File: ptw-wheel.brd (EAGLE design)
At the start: 54 x 45 mm, 4 parts

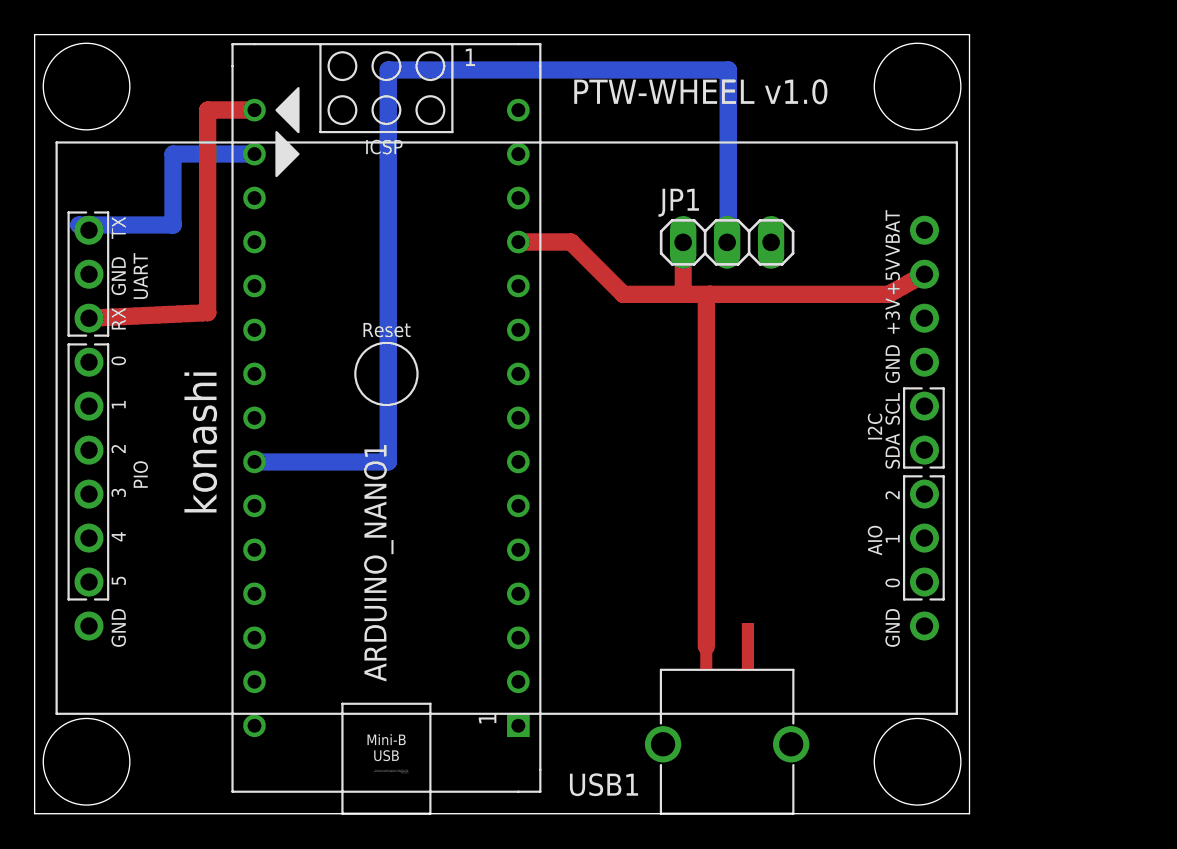
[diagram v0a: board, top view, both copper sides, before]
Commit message: GNDがAirwireになっているのを解消できた！
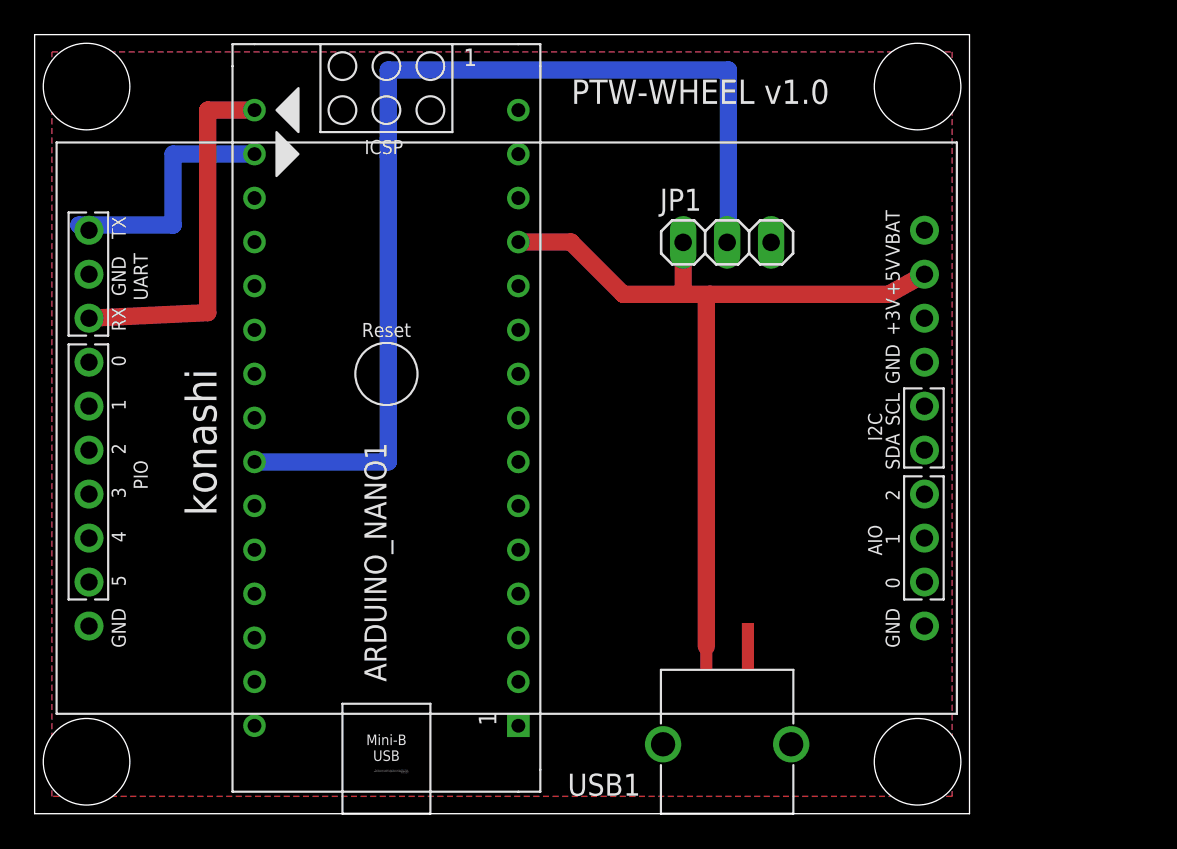
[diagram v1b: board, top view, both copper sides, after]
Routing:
- added copper zone on layer 1, net GND
- added copper zone on layer 16, net GND
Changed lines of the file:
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@@
 <contactref element="U$1" pad="GND@3"/>
 <contactref element="U$1" pad="GND@2"/>
-<wire x1="12.7" y1="33.02" x2="42.54" y2="33" width="0" layer="19" extent="1-16"/>
-<wire x1="42.54" y1="33" x2="51.4" y2="10.84" width="0" layer="19" extent="1-16"/>
-<wire x1="51.4" y1="10.84" x2="51.4" y2="26.08" width="0" layer="19" extent="1-16"/>
-<wire x1="51.4" y1="26.08" x2="3.14" y2="10.84" width="0" layer="19" extent="1-16"/>
-<wire x1="3.14" y1="10.84" x2="41.2" y2="9.66" width="0" layer="19" extent="1-16"/>
-<wire x1="41.2" y1="9.66" x2="43.7" y2="4.01" width="0" layer="19" extent="1-16"/>
-<wire x1="43.7" y1="4.01" x2="36.3" y2="4.01" width="0" layer="19" extent="1-16"/>
-<wire x1="27.94" y1="38.1" x2="3.14" y2="31.16" width="0" layer="19" extent="1-16"/>
+<polygon width="1" layer="16">
+<vertex x="1" y="44"/>
+<vertex x="53" y="44"/>
+<vertex x="53" y="1"/>
+<vertex x="1" y="1"/>
+</polygon>
+<polygon width="1" layer="1">
+<vertex x="1" y="44"/>
+<vertex x="53" y="44"/>
+<vertex x="53" y="1"/>
+<vertex x="1" y="1"/>
+</polygon>
 </signal>
 </signals>

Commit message: 更新
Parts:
- removed U$1: KONASHI2.0, konashiv2-withoud_drill_hole:KONASHI
- added KONASHI: KONASHI2.0, konashiv2-withoud_drill_hole:KONASHI
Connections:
- net +3V: now also KONASHI.+3V; no longer U$1.+3V
- net +5V: now also KONASHI.+5V; no longer U$1.+5V
- net GND: now also KONASHI.GND, KONASHI.GND@1, KONASHI.GND@2, KONASHI.GND@3; no longer U$1.GND, U$1.GND@1, U$1.GND@2, U$1.GND@3
- net N$4: now also KONASHI.TX; no longer U$1.TX
- net N$5: now also KONASHI.RX; no longer U$1.RX
- net VBAT: now also KONASHI.VBAT; no longer U$1.VBAT
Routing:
- removed copper zone on layer 1, net GND
- removed copper zone on layer 16, net GND
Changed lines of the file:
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@@
 <attribute name="VALUE" x="36.19" y="29.825" size="1.27" layer="27"/>
 </element>
-<element name="U$1" library="konashiv2-withoud_drill_hole" package="KONASHI" value="KONASHI2.0" x="26" y="21" smashed="yes" rot="R90"/>
+<element name="KONASHI" library="konashiv2-withoud_drill_hole" package="KONASHI" value="KONASHI2.0" x="25.6" y="21.2" smashed="yes" rot="R90"/>
 <element name="USB1" library="usbcon" package="USBCON" value="USBCON" x="40" y="8.31" smashed="yes" rot="R180">
 <attribute name="NAME" x="35" y="2.31" size="1.27" layer="25" rot="R180"/>
@@
 <signals>
 <signal name="+3V">
-<contactref element="U$1" pad="+3V"/>
+<contactref element="KONASHI" pad="+3V"/>
 </signal>
 <signal name="VBAT">
-<contactref element="U$1" pad="VBAT"/>
+<contactref element="KONASHI" pad="VBAT"/>
 </signal>
 <signal name="VIN">
@@
 </signal>
 <signal name="N$4">
-<contactref element="U$1" pad="TX"/>
+<contactref element="KONASHI" pad="TX"/>
 <contactref element="ARDUINO_NANO1" pad="17"/>
 <wire x1="12.7" y1="38.1" x2="8" y2="38.1" width="1" layer="16"/>
 <wire x1="8" y1="38.1" x2="8" y2="34" width="1" layer="16"/>
-<wire x1="8" y1="34" x2="2.56" y2="34" width="1" layer="16"/>
-<wire x1="2.56" y1="34" x2="3.14" y2="33.7" width="1" layer="16"/>
+<wire x1="8" y1="34" x2="2.546665625" y2="34" width="1" layer="16"/>
+<wire x1="2.546665625" y1="34" x2="2.74" y2="33.9" width="1" layer="16"/>
 </signal>
 <signal name="N$5">
-<contactref element="U$1" pad="RX"/>
+<contactref element="KONASHI" pad="RX"/>
 <contactref element="ARDUINO_NANO1" pad="16"/>
-<wire x1="3.14" y1="28.62" x2="10" y2="28.94" width="1" layer="1"/>
-<wire x1="10" y1="28.94" x2="10" y2="40.629840625" width="1" layer="1"/>
+<wire x1="2.74" y1="28.82" x2="10" y2="29.158659375" width="1" layer="1"/>
+<wire x1="10" y1="29.158659375" x2="10" y2="40.629840625" width="1" layer="1"/>
 <wire x1="10.010159375" y1="40.64" x2="10" y2="40.629840625" width="1" layer="1"/>
 <wire x1="10.010159375" y1="40.64" x2="12.7" y2="40.64" width="1" layer="1"/>
@@
 <signal name="+5V">
 <contactref element="USB1" pad="5V"/>
-<contactref element="U$1" pad="+5V"/>
+<contactref element="KONASHI" pad="+5V"/>
 <contactref element="JP1" pad="1"/>
 <contactref element="ARDUINO_NANO1" pad="12"/>
@@
 <wire x1="37.462459375" y1="32.997540625" x2="37.46" y2="33" width="1" layer="1"/>
 <wire x1="37.462459375" y1="30" x2="39" y2="30" width="1" layer="1"/>
-<wire x1="39" y1="30" x2="49.32" y2="30" width="1" layer="1"/>
-<wire x1="49.32" y1="30" x2="51.4" y2="31.16" width="1" layer="1"/>
+<wire x1="39" y1="30" x2="48.561378125" y2="30" width="1" layer="1"/>
+<wire x1="48.561378125" y1="30" x2="51" y2="31.36" width="1" layer="1"/>
 <wire x1="38.8" y1="9.66" x2="38.8" y2="29.8" width="1" layer="1"/>
 <wire x1="38.8" y1="29.8" x2="39" y2="30" width="1" layer="1"/>
 </signal>
 <signal name="GND">
-<contactref element="U$1" pad="GND"/>
+<contactref element="KONASHI" pad="GND"/>
 <contactref element="USB1" pad="GND"/>
 <contactref element="USB1" pad="SHIELD1"/>
 <contactref element="USB1" pad="SHIELD2"/>
-<contactref element="U$1" pad="GND@1"/>
+<contactref element="KONASHI" pad="GND@1"/>
 <contactref element="JP1" pad="3"/>
 <contactref element="ARDUINO_NANO1" pad="19"/>
 <contactref element="ARDUINO_NANO1" pad="14"/>
-<contactref element="U$1" pad="GND@3"/>
-<contactref element="U$1" pad="GND@2"/>
-<polygon width="1" layer="16">
-<vertex x="1" y="44"/>
-<vertex x="53" y="44"/>
-<vertex x="53" y="1"/>
-<vertex x="1" y="1"/>
-</polygon>
-<polygon width="1" layer="1">
-<vertex x="1" y="44"/>
-<vertex x="53" y="44"/>
-<vertex x="53" y="1"/>
-<vertex x="1" y="1"/>
-</polygon>
+<contactref element="KONASHI" pad="GND@3"/>
+<contactref element="KONASHI" pad="GND@2"/>
+<wire x1="42.54" y1="33" x2="51" y2="26.28" width="0" layer="19" extent="1-1"/>
+<wire x1="51" y1="26.28" x2="51" y2="11.04" width="0" layer="19" extent="1-1"/>
+<wire x1="41.2" y1="9.66" x2="51" y2="11.04" width="0" layer="19" extent="1-1"/>
+<wire x1="43.7" y1="4.01" x2="41.2" y2="9.66" width="0" layer="19" extent="1-1"/>
+<wire x1="36.3" y1="4.01" x2="43.7" y2="4.01" width="0" layer="19" extent="1-1"/>
+<wire x1="27.94" y1="38.1" x2="42.54" y2="33" width="0" layer="19" extent="1-1"/>
+<wire x1="12.7" y1="33.02" x2="27.94" y2="38.1" width="0" layer="19" extent="1-1"/>
+<wire x1="2.74" y1="31.36" x2="12.7" y2="33.02" width="0" layer="19" extent="1-1"/>
+<wire x1="2.74" y1="11.04" x2="2.74" y2="31.36" width="0" layer="19" extent="1-1"/>
 </signal>
 </signals>

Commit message: ボードのレイアウト整理
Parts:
- moved KONASHI 0.13 mm to (25.7, 21.2)
- renumbered ARDUINO_NANO1 to ARDUINO_NANO, USB1 to USB
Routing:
- net GND: track 0.00 -> 133.8 mm
- net N$3: track 60.0 -> 62.2 mm
- added copper zone on layer 1, net GND
- added copper zone on layer 16, net GND
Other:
- board text added: "GND"

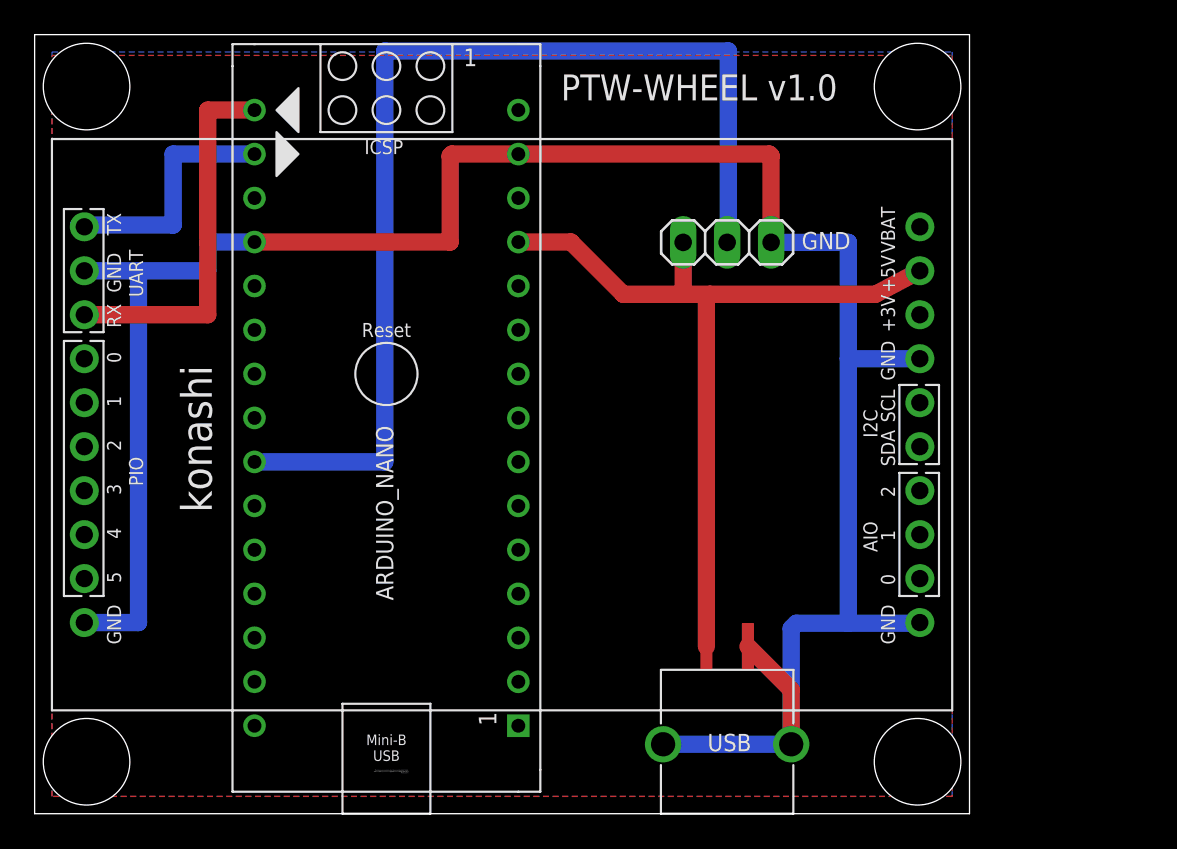
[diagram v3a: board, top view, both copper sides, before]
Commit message: トグルスイッチを追加
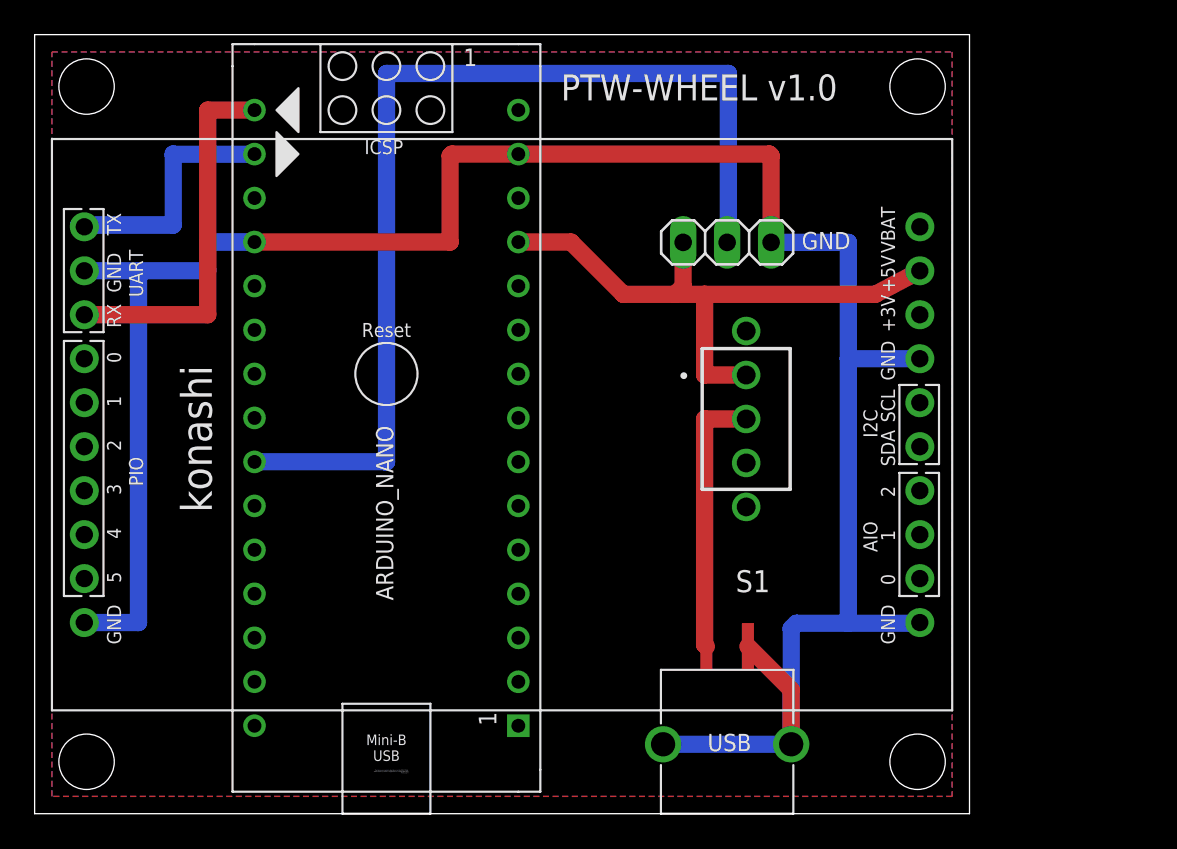
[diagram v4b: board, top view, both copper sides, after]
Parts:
- added S1: 2MS1-T1-B4-M2-Q-E, 2MS1-T1-B4-VS2-Q-E:2MS1-T1-B4-M2-Q-E
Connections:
- new net N$1: S1.2, USB.5V
- net +5V: now also S1.1; no longer USB.5V
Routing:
- net N$1: track 0.00 -> 15.6 mm
- net +5V: track 48.2 -> 35.0 mm
- net N$3: track 62.2 -> 59.6 mm
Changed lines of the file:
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@@
 <layer number="49" name="Reference" color="7" fill="1" visible="yes" active="yes"/>
 <layer number="50" name="dxf" color="12" fill="1" visible="no" active="no"/>
-<layer number="51" name="tDocu" color="7" fill="1" visible="yes" active="yes"/>
+<layer number="51" name="tDocu" color="7" fill="1" visible="no" active="yes"/>
 <layer number="52" name="bDocu" color="7" fill="1" visible="yes" active="yes"/>
 <layer number="53" name="tGND_GNDA" color="7" fill="9" visible="no" active="no"/>
@@
 <wire x1="54" y1="45" x2="0" y2="45" width="0" layer="20"/>
 <wire x1="0" y1="45" x2="0" y2="0" width="0" layer="20"/>
-<hole x="3" y="42" drill="5"/>
-<hole x="3" y="3" drill="5"/>
-<hole x="51" y="3" drill="5"/>
-<hole x="51" y="42" drill="5"/>
+<hole x="3" y="42" drill="3.2"/>
+<hole x="3" y="3" drill="3.2"/>
+<hole x="51" y="3" drill="3.2"/>
+<hole x="51" y="42" drill="3.2"/>
 <text x="30.4" y="41.2" size="1.5" layer="25">PTW-WHEEL v1.0</text>
 <text x="44.3" y="32.6" size="1" layer="25">GND</text>
@@
 <attribute name="NAME" x="41.4" y="4.61" size="1" layer="25" rot="R180"/>
 </element>
+<element name="S1" library="2MS1-T1-B4-VS2-Q-E" package="2MS1-T1-B4-M2-Q-E" value="2MS1-T1-B4-M2-Q-E" x="41.1" y="22.8" smashed="yes" rot="R180">
+<attribute name="DESCRIPTION" value="Sub-miniature toggle switch" x="41.1" y="22.8" size="1" layer="27" rot="R180" display="off"/>
+<attribute name="HEIGHT" value="mm" x="41.1" y="22.8" size="1" layer="27" rot="R180" display="off"/>
+<attribute name="MANUFACTURER_NAME" value="Cosland" x="41.1" y="22.8" size="1" layer="27" rot="R180" display="off"/>
+<attribute name="MANUFACTURER_PART_NUMBER" value="2MS1-T1-B4-M2-Q-E" x="41.1" y="22.8" size="1" layer="27" rot="R180" display="off"/>
+<attribute name="MOUSER_PART_NUMBER" value="" x="41.1" y="22.8" size="1" layer="27" rot="R180" display="off"/>
+<attribute name="MOUSER_PRICE-STOCK" value="" x="41.1" y="22.8" size="1" layer="27" rot="R180" display="off"/>
+<attribute name="NAME" x="41.489" y="13.429" size="1.27" layer="25" rot="R180" align="center"/>
+<attribute name="RS_PART_NUMBER" value="" x="41.1" y="22.8" size="1" layer="27" rot="R180" display="off"/>
+<attribute name="RS_PRICE-STOCK" value="" x="41.1" y="22.8" size="1" layer="27" rot="R180" display="off"/>
+<attribute name="VALUE" x="41.489" y="14.842" size="1.27" layer="27" rot="R180" align="center"/>
+</element>
 </elements>
 <signals>
@@
 <contactref element="JP1" pad="2"/>
 <contactref element="ARDUINO_NANO" pad="24"/>
-<wire x1="12.7" y1="20.32" x2="20.22668125" y2="20.32" width="1" layer="16"/>
-<wire x1="20.22668125" y1="44.05648125" x2="20.22668125" y2="20.32" width="1" layer="16"/>
-<wire x1="20.22668125" y1="44.05648125" x2="40.071040625" y2="44.05648125" width="1" layer="16"/>
-<wire x1="40.071040625" y1="44.05648125" x2="40.071040625" y2="33.071040625" width="1" layer="16"/>
+<wire x1="12.7" y1="20.32" x2="20.32668125" y2="20.32" width="1" layer="16"/>
+<wire x1="20.32668125" y1="42.75648125" x2="20.32668125" y2="20.32" width="1" layer="16"/>
+<wire x1="20.32668125" y1="42.75648125" x2="40.071040625" y2="42.75648125" width="1" layer="16"/>
+<wire x1="40.071040625" y1="42.75648125" x2="40.071040625" y2="33.071040625" width="1" layer="16"/>
 <wire x1="40.071040625" y1="33.071040625" x2="40" y2="33" width="1" layer="16"/>
 </signal>
@@
 </signal>
 <signal name="+5V">
-<contactref element="USB" pad="5V"/>
 <contactref element="KONASHI" pad="+5V"/>
 <contactref element="JP1" pad="1"/>
@@
 <wire x1="27.94" y1="33.02" x2="30.98" y2="33.02" width="1" layer="1"/>
 <wire x1="30.98" y1="33.02" x2="34" y2="30" width="1" layer="1"/>
-<wire x1="34" y1="30" x2="37.462459375" y2="30" width="1" layer="1"/>
-<wire x1="37.462459375" y1="30" x2="37.462459375" y2="32.997540625" width="1" layer="1"/>
-<wire x1="37.462459375" y1="32.997540625" x2="37.46" y2="33" width="1" layer="1"/>
-<wire x1="37.462459375" y1="30" x2="39" y2="30" width="1" layer="1"/>
-<wire x1="39" y1="30" x2="48.561378125" y2="30" width="1" layer="1"/>
-<wire x1="48.561378125" y1="30" x2="51.13" y2="31.36" width="1" layer="1"/>
-<wire x1="38.8" y1="9.66" x2="38.8" y2="29.8" width="1" layer="1"/>
-<wire x1="38.8" y1="29.8" x2="39" y2="30" width="1" layer="1"/>
+<wire x1="51.13" y1="31.36" x2="48.561378125" y2="30" width="1" layer="1"/>
+<contactref element="S1" pad="1"/>
+<wire x1="41.1" y1="25.34" x2="38.701" y2="25.34" width="1" layer="1"/>
+<wire x1="48.561378125" y1="30" x2="38.701" y2="30" width="1" layer="1"/>
+<wire x1="38.701" y1="25.34" x2="38.701" y2="30" width="1" layer="1"/>
+<wire x1="34" y1="30" x2="37" y2="30" width="1" layer="1"/>
+<wire x1="37" y1="30" x2="38.701" y2="30" width="1" layer="1"/>
+<wire x1="37.46" y1="33" x2="37.46" y2="30.46" width="1" layer="1"/>
+<wire x1="37.46" y1="30.46" x2="37" y2="30" width="1" layer="1"/>
 </signal>
 <signal name="GND">
@@
 <wire x1="43.7" y1="4.01" x2="43.7" y2="10.7" width="1" layer="16"/>
 <wire x1="43.7" y1="10.7" x2="44" y2="11" width="1" layer="16"/>
+<wire x1="41.2" y1="9.66" x2="43.7" y2="7.16" width="1" layer="1"/>
+<wire x1="43.7" y1="7.16" x2="43.7" y2="4.01" width="1" layer="1"/>
+<wire x1="36.3" y1="4.01" x2="43.7" y2="4.01" width="1" layer="16"/>
+<polygon width="1" layer="1">
+<vertex x="1" y="44"/>
+<vertex x="53" y="44"/>
+<vertex x="53" y="1"/>
+<vertex x="1" y="1"/>
+</polygon>
 <polygon width="1" layer="16">
 <vertex x="1" y="44"/>
@@
 <vertex x="1" y="1"/>
 </polygon>
-<polygon width="1" layer="1">
-<vertex x="1" y="43.8"/>
-<vertex x="53" y="43.8"/>
-<vertex x="53" y="1"/>
-<vertex x="1" y="1"/>
-</polygon>
-<wire x1="41.2" y1="9.66" x2="43.7" y2="7.16" width="1" layer="1"/>
-<wire x1="43.7" y1="7.16" x2="43.7" y2="4.01" width="1" layer="1"/>
-<wire x1="36.3" y1="4.01" x2="43.7" y2="4.01" width="1" layer="16"/>
+</signal>
+<signal name="N$1">
+<contactref element="USB" pad="5V"/>
+<contactref element="S1" pad="2"/>
+<wire x1="41.1" y1="22.8" x2="38.7" y2="22.8" width="1" layer="1"/>
+<wire x1="38.7" y1="22.8" x2="38.7" y2="9.76" width="1" layer="1"/>
+<wire x1="38.7" y1="9.76" x2="38.8" y2="9.66" width="1" layer="1"/>
 </signal>
 </signals>

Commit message: 調整
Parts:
- ARDUINO_NANO: device arduinoNanoV30-withoud_drill_hole:ARDUINO_NANO -> ArduinoNanoV30:ARDUINO_NANO
- JP1: value LED tapes -> LED tape
- KONASHI: device konashiv2-withoud_drill_hole:KONASHI -> konashiv2:KONASHI
- moved KONASHI 29.0 mm to (1.00, 6.00), turned to 0 degrees
- moved S1 1.00 mm to (41.1, 21.8)
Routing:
- net +5V: track 35.0 -> 36.3 mm
- net N$1: track 15.6 -> 14.6 mm
- net GND: track 133.8 -> 134.8 mm
- net N$4: track 14.6 -> 13.9 mm
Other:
- board text added: "OFF"
- board text added: "ON"
- board text added: "PTW-WHEEL v1.1"
- board text removed: "PTW-WHEEL v1.0"
